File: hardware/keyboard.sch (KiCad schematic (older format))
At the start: 21 parts, among them J1 USB_OTG, J2 CONN_02X09, U1 ATMEGA32U4-AU, Y1 16MHz

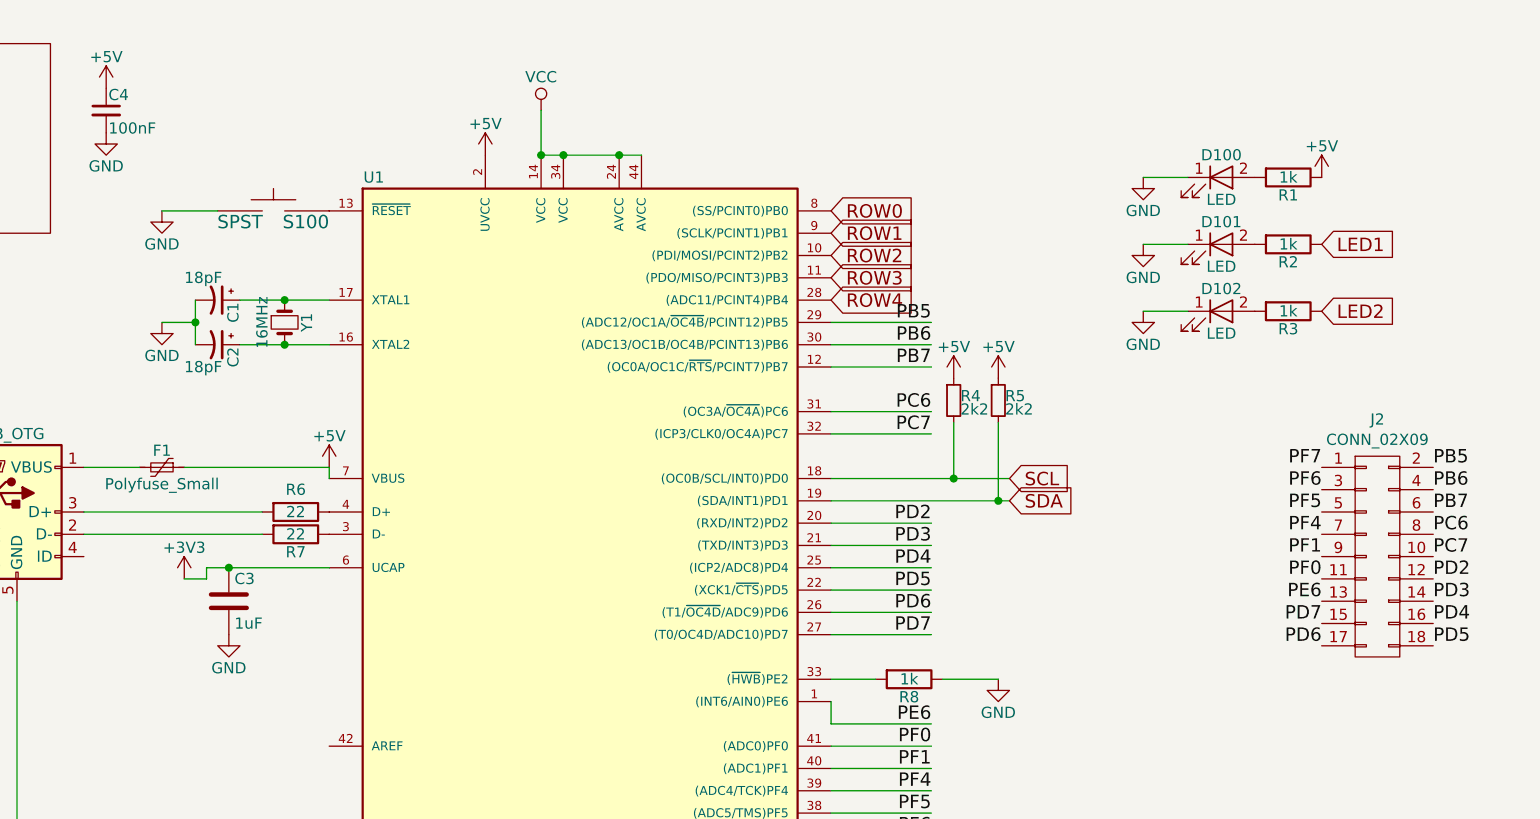
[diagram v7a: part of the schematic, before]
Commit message: Start to lay out components
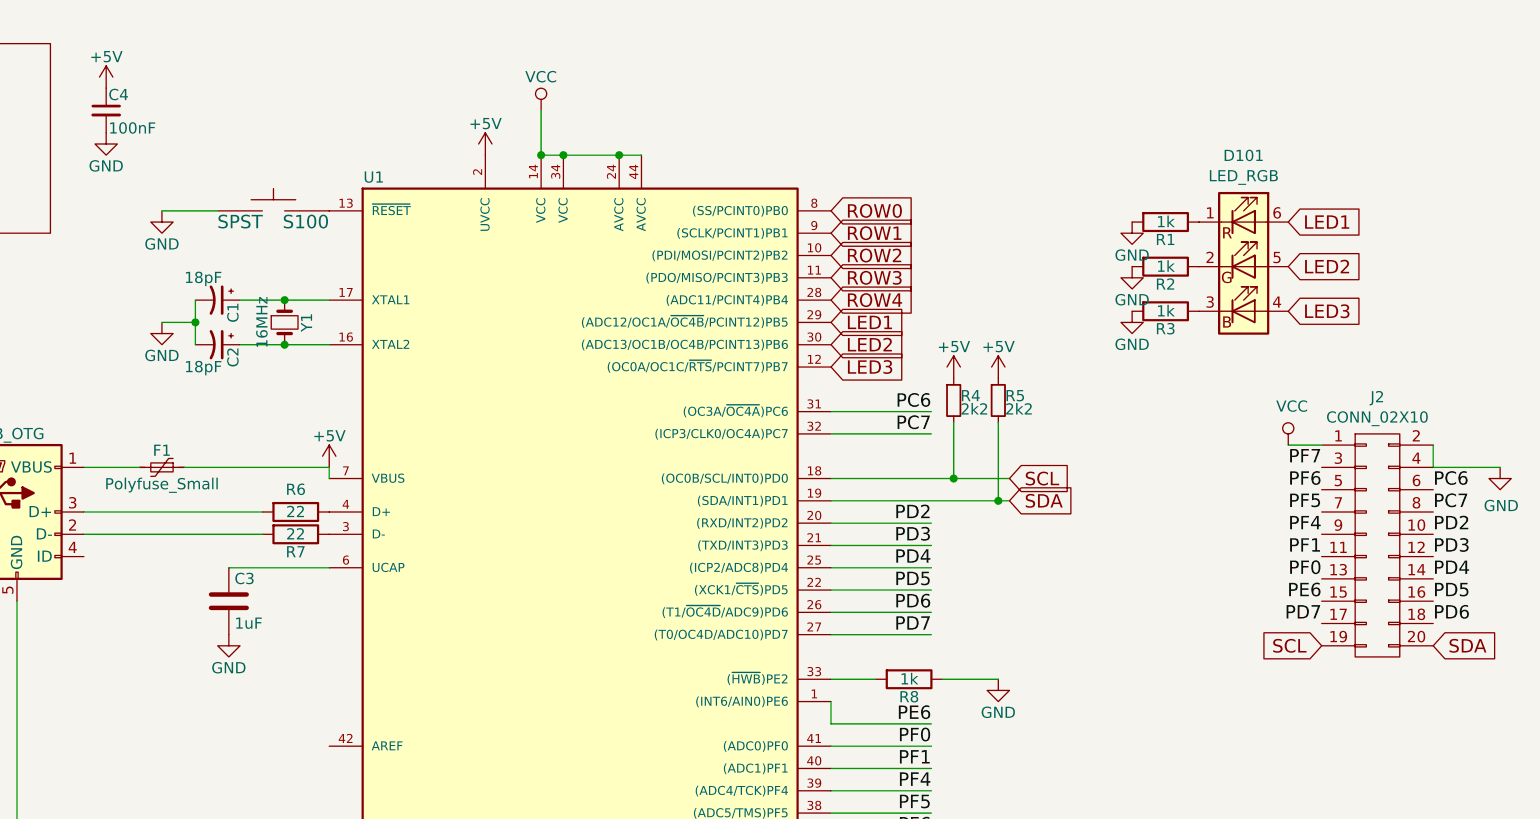
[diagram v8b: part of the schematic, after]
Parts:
- removed D100, D101, D102: LED, LEDs:LED_1206, symbol LED
- removed J2: CONN_02X09, keyboard-modules:pads, symbol CONN_02X09
- added D101: LED_RGB, LEDs:LED_RGB_5050-6, symbol LED_RGB
- added J2: CONN_02X10, keyboard-modules:ExpansionPads, symbol CONN_02X10
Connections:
- net PB5 is gone; now on net LED1: U1.29 ((ADC12/OC1A/~OC4B~/PCINT12)PB5)
- net PB6 is gone; now on net LED2: U1.30 ((ADC13/OC1B/OC4B/PCINT13)PB6)
- net +5V: no longer R1.1
- net GND: now also R1.2, R2.2, R3.2, J2.2 (P2), J2.4 (P4)
- net LED1: now also D101.6 (RA); no longer R2.1
- net LED2: now also D101.5 (GA); no longer R3.1
- net PC6: now also J2.6 (P6)
- net PC7: now also J2.8 (P8)
- net PD2: now also J2.10 (P10)
- net PD3: now also J2.12 (P12)
- net PD4: now also J2.14 (P14)
- net PD5: now also J2.16 (P16)
- net PD6: now also J2.18 (P18)
- net PD7: now also J2.17 (P17)
- net PE6: now also J2.15 (P15)
- net PF0: now also J2.13 (P13)
- net PF1: now also J2.11 (P11)
- net PF4: now also J2.9 (P9)
- net PF5: now also J2.7 (P7)
- net PF6: now also J2.5 (P5)
- net PF7: now also J2.3 (P3)
- net SCL: now also J2.19 (P19)
- net SDA: now also J2.20 (P20)
- net VCC: now also J2.1 (P1)
- net +3V3: no longer names the net of C3.1, U1.6 (UCAP)
- net PB7 renamed LED3
- net LED3: now also D101.4 (BA)
- new net: D101.1 (RK), R1.1
- new net: D101.2 (GK), R2.1
- new net: D101.3 (BK), R3.1
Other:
- moved on the sheet: R1, R2, R3
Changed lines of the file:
@@
 LIBS:valves
 LIBS:keyboard-cache
-EELAYER 25 0
+EELAYER 26 0
 EELAYER END
 $Descr A4 11693 8268
@@
 $EndComp
 $Comp
-L +3V3 #PWR04
-U 1 1 58EC69E9
-P 2150 3000
-F 0 "#PWR04" H 2150 2850 50  0001 C CNN
-F 1 "+3V3" H 2150 3140 50  0000 C CNN
-F 2 "" H 2150 3000 50  0001 C CNN
-F 3 "" H 2150 3000 50  0001 C CNN
-	1    2150 3000
-	1    0    0    -1
-$EndComp
-$Comp
-L LED D100
-U 1 1 58EC6D5A
-P 6800 1200
-F 0 "D100" H 6800 1300 50  0000 C CNN
-F 1 "LED" H 6800 1100 50  0000 C CNN
-F 2 "LEDs:LED_1206" H 6800 1200 50  0001 C CNN
-F 3 "" H 6800 1200 50  0001 C CNN
-	1    6800 1200
-	1    0    0    -1
-$EndComp
-$Comp
-L GND #PWR05
+L GND #PWR04
 U 1 1 58EC7101
-P 6450 1200
-F 0 "#PWR05" H 6450 950 50  0001 C CNN
-F 1 "GND" H 6450 1050 50  0000 C CNN
-F 2 "" H 6450 1200 50  0001 C CNN
-F 3 "" H 6450 1200 50  0001 C CNN
-	1    6450 1200
-	1    0    0    -1
-$EndComp
-$Comp
-L +5V #PWR06
-U 1 1 58EC7227
-P 7250 1200
-F 0 "#PWR06" H 7250 1050 50  0001 C CNN
-F 1 "+5V" H 7250 1340 50  0000 C CNN
-F 2 "" H 7250 1200 50  0001 C CNN
-F 3 "" H 7250 1200 50  0001 C CNN
-	1    7250 1200
+P 6400 1400
+F 0 "#PWR04" H 6400 1150 50  0001 C CNN
+F 1 "GND" H 6400 1250 50  0000 C CNN
+F 2 "" H 6400 1400 50  0001 C CNN
+F 3 "" H 6400 1400 50  0001 C CNN
+	1    6400 1400
 	1    0    0    -1
 $EndComp
@@
 L R R1
 U 1 1 58EC77A9
-P 7100 1200
-F 0 "R1" V 7180 1200 50  0000 C CNN
-F 1 "1k" V 7100 1200 50  0000 C CNN
-F 2 "Resistors_SMD:R_1206_HandSoldering" V 7030 1200 50  0001 C CNN
-F 3 "" H 7100 1200 50  0001 C CNN
-	1    7100 1200
+P 6550 1400
+F 0 "R1" V 6630 1400 50  0000 C CNN
+F 1 "1k" V 6550 1400 50  0000 C CNN
+F 2 "Resistors_SMD:R_1206_HandSoldering" V 6480 1400 50  0001 C CNN
+F 3 "" H 6550 1400 50  0001 C CNN
+	1    6550 1400
 	0    1    1    0
 $EndComp
@@
 $EndComp
 $Comp
-L GND #PWR07
+L GND #PWR05
 U 1 1 58EC962F
 P 2050 1850
-F 0 "#PWR07" H 2050 1600 50  0001 C CNN
+F 0 "#PWR05" H 2050 1600 50  0001 C CNN
 F 1 "GND" H 2050 1700 50  0000 C CNN
 F 2 "" H 2050 1850 50  0001 C CNN
@@
 $EndComp
 $Comp
-L +5V #PWR08
+L +5V #PWR06
 U 1 1 58ED0C76
 P 2800 2500
-F 0 "#PWR08" H 2800 2350 50  0001 C CNN
+F 0 "#PWR06" H 2800 2350 50  0001 C CNN
 F 1 "+5V" H 2800 2640 50  0000 C CNN
 F 2 "" H 2800 2500 50  0001 C CNN
@@
 $EndComp
 $Comp
-L +5V #PWR09
+L +5V #PWR07
 U 1 1 58ED0DA2
 P 3500 1100
-F 0 "#PWR09" H 3500 950 50  0001 C CNN
+F 0 "#PWR07" H 3500 950 50  0001 C CNN
 F 1 "+5V" H 3500 1240 50  0000 C CNN
 F 2 "" H 3500 1100 50  0001 C CNN
@@
 Connection ~ 3800 4500
 Wire Wire Line
-	2250 2950 2800 2950
-Wire Wire Line
-	2150 3000 2250 3000
-Wire Wire Line
-	2250 3000 2250 2950
-Connection ~ 2350 2950
-Wire Wire Line
-	6650 1200 6450 1200
+	2350 2950 2800 2950
 Wire Wire Line
 	2400 1750 2800 1750
@@
 Connection ~ 5800 2650
 $Comp
-L +5V #PWR010
+L +5V #PWR08
 U 1 1 594E98E9
 P 5600 2100
-F 0 "#PWR010" H 5600 1950 50  0001 C CNN
+F 0 "#PWR08" H 5600 1950 50  0001 C CNN
 F 1 "+5V" H 5600 2240 50  0000 C CNN
 F 2 "" H 5600 2100 50  0001 C CNN
@@
 $EndComp
 $Comp
-L +5V #PWR011
+L +5V #PWR09
 U 1 1 594E9917
 P 5800 2100
-F 0 "#PWR011" H 5800 1950 50  0001 C CNN
+F 0 "#PWR09" H 5800 1950 50  0001 C CNN
 F 1 "+5V" H 5800 2240 50  0000 C CNN
 F 2 "" H 5800 2100 50  0001 C CNN
@@
 $EndComp
 $Comp
-L LED D101
-U 1 1 594E9DFB
-P 6800 1500
-F 0 "D101" H 6800 1600 50  0000 C CNN
-F 1 "LED" H 6800 1400 50  0000 C CNN
-F 2 "LEDs:LED_1206" H 6800 1500 50  0001 C CNN
-F 3 "" H 6800 1500 50  0001 C CNN
-	1    6800 1500
-	1    0    0    -1
-$EndComp
-$Comp
-L GND #PWR012
+L GND #PWR010
 U 1 1 594E9E01
-P 6450 1500
-F 0 "#PWR012" H 6450 1250 50  0001 C CNN
-F 1 "GND" H 6450 1350 50  0000 C CNN
-F 2 "" H 6450 1500 50  0001 C CNN
-F 3 "" H 6450 1500 50  0001 C CNN
-	1    6450 1500
+P 6400 1600
+F 0 "#PWR010" H 6400 1350 50  0001 C CNN
+F 1 "GND" H 6400 1450 50  0000 C CNN
+F 2 "" H 6400 1600 50  0001 C CNN
+F 3 "" H 6400 1600 50  0001 C CNN
+	1    6400 1600
 	1    0    0    -1
 $EndComp
@@
 L R R2
 U 1 1 594E9E0D
-P 7100 1500
-F 0 "R2" V 7180 1500 50  0000 C CNN
-F 1 "1k" V 7100 1500 50  0000 C CNN
-F 2 "Resistors_SMD:R_1206_HandSoldering" V 7030 1500 50  0001 C CNN
-F 3 "" H 7100 1500 50  0001 C CNN
-	1    7100 1500
-	0    1    1    0
-$EndComp
-Wire Wire Line
-	6650 1500 6450 1500
-$Comp
-L LED D102
-U 1 1 594E9E7C
-P 6800 1800
-F 0 "D102" H 6800 1900 50  0000 C CNN
-F 1 "LED" H 6800 1700 50  0000 C CNN
-F 2 "LEDs:LED_1206" H 6800 1800 50  0001 C CNN
-F 3 "" H 6800 1800 50  0001 C CNN
-	1    6800 1800
-	1    0    0    -1
-$EndComp
-$Comp
-L GND #PWR013
+P 6550 1600
+F 0 "R2" V 6630 1600 50  0000 C CNN
+F 1 "1k" V 6550 1600 50  0000 C CNN
+F 2 "Resistors_SMD:R_1206_HandSoldering" V 6480 1600 50  0001 C CNN
+F 3 "" H 6550 1600 50  0001 C CNN
+	1    6550 1600
+	0    1    1    0
+$EndComp
+$Comp
+L GND #PWR011
 U 1 1 594E9E82
-P 6450 1800
-F 0 "#PWR013" H 6450 1550 50  0001 C CNN
-F 1 "GND" H 6450 1650 50  0000 C CNN
-F 2 "" H 6450 1800 50  0001 C CNN
-F 3 "" H 6450 1800 50  0001 C CNN
-	1    6450 1800
+P 6400 1800
+F 0 "#PWR011" H 6400 1550 50  0001 C CNN
+F 1 "GND" H 6400 1650 50  0000 C CNN
+F 2 "" H 6400 1800 50  0001 C CNN
+F 3 "" H 6400 1800 50  0001 C CNN
+	1    6400 1800
 	1    0    0    -1
 $EndComp
@@
 L R R3
 U 1 1 594E9E8E
-P 7100 1800
-F 0 "R3" V 7180 1800 50  0000 C CNN
-F 1 "1k" V 7100 1800 50  0000 C CNN
-F 2 "Resistors_SMD:R_1206_HandSoldering" V 7030 1800 50  0001 C CNN
-F 3 "" H 7100 1800 50  0001 C CNN
-	1    7100 1800
-	0    1    1    0
-$EndComp
-Wire Wire Line
-	6650 1800 6450 1800
-Text GLabel 7250 1500 2    60   Input ~ 0
+P 6550 1800
+F 0 "R3" V 6630 1800 50  0000 C CNN
+F 1 "1k" V 6550 1800 50  0000 C CNN
+F 2 "Resistors_SMD:R_1206_HandSoldering" V 6480 1800 50  0001 C CNN
+F 3 "" H 6550 1800 50  0001 C CNN
+	1    6550 1800
+	0    1    1    0
+$EndComp
+Text GLabel 7100 1400 2    60   Input ~ 0
 LED1
-Text GLabel 7250 1800 2    60   Input ~ 0
+Text GLabel 7100 1600 2    60   Input ~ 0
 LED2
 $Comp
@@
 	5050 3450 5250 3450
 $Comp
-L GND #PWR014
+L GND #PWR012
 U 1 1 594EA1C7
 P 5800 3450
-F 0 "#PWR014" H 5800 3200 50  0001 C CNN
+F 0 "#PWR012" H 5800 3200 50  0001 C CNN
 F 1 "GND" H 5800 3300 50  0000 C CNN
 F 2 "" H 5800 3450 50  0001 C CNN
@@
 	5550 3450 5800 3450
 $Comp
-L GND #PWR015
+L GND #PWR013
 U 1 1 594EA3EB
 P 2050 1350
-F 0 "#PWR015" H 2050 1100 50  0001 C CNN
+F 0 "#PWR013" H 2050 1100 50  0001 C CNN
 F 1 "GND" H 2050 1200 50  0000 C CNN
 F 2 "" H 2050 1350 50  0001 C CNN
@@
 	2300 1350 2050 1350
 Wire Wire Line
-	5050 1850 5500 1850
-Wire Wire Line
-	5050 1950 5500 1950
-Wire Wire Line
-	5050 2050 5500 2050
-Wire Wire Line
 	5050 2250 5500 2250
 Wire Wire Line
@@
 Wire Wire Line
 	5050 4250 5500 4250
-Text Label 5500 1850 2    60   ~ 0
-PB5
-Text Label 5500 1950 2    60   ~ 0
-PB6
-Text Label 5500 2050 2    60   ~ 0
-PB7
 Text Label 5500 2250 2    60   ~ 0
 PC6
@@
 Text Label 5500 4250 2    60   ~ 0
 PF7
-Text Label 7750 2500 0    60   ~ 0
-PB5
 Text Label 7750 2600 0    60   ~ 0
-PB6
+PC6
 Text Label 7750 2700 0    60   ~ 0
-PB7
+PC7
 Text Label 7750 2800 0    60   ~ 0
-PC6
+PD2
 Text Label 7750 2900 0    60   ~ 0
-PC7
+PD3
 Text Label 7750 3000 0    60   ~ 0
-PD2
+PD4
 Text Label 7750 3100 0    60   ~ 0
-PD3
+PD5
 Text Label 7750 3200 0    60   ~ 0
-PD4
-Text Label 7750 3300 0    60   ~ 0
-PD5
-Text Label 7250 3300 2    60   ~ 0
 PD6
 Text Label 7250 3200 2    60   ~ 0
@@
 $EndComp
 $Comp
-L +5V #PWR016
+L +5V #PWR014
 U 1 1 5955BD4A
 P 1800 800
-F 0 "#PWR016" H 1800 650 50  0001 C CNN
+F 0 "#PWR014" H 1800 650 50  0001 C CNN
 F 1 "+5V" H 1800 940 50  0000 C CNN
 F 2 "" H 1800 800 50  0001 C CNN
@@
 $EndComp
 $Comp
-L GND #PWR017
+L GND #PWR015
 U 1 1 5955BE42
 P 1800 1000
-F 0 "#PWR017" H 1800 750 50  0001 C CNN
+F 0 "#PWR015" H 1800 750 50  0001 C CNN
 F 1 "GND" H 1800 850 50  0000 C CNN
 F 2 "" H 1800 1000 50  0001 C CNN
@@
 $EndComp
 $Comp
-L CONN_02X09 J2
-U 1 1 595846BC
-P 7500 2900
+L LED_RGB D101
+U 1 1 595A9E52
+P 6900 1600
+F 0 "D101" H 6900 2097 50  0000 C CNN
+F 1 "LED_RGB" H 6900 2006 50  0000 C CNN
+F 2 "LEDs:LED_RGB_5050-6" H 6900 1550 50  0001 C CNN
+F 3 "" H 6900 1550 50  0001 C CNN
+	1    6900 1600
+	1    0    0    -1
+$EndComp
+Text GLabel 7100 1800 2    60   Input ~ 0
+LED3
+Text GLabel 5050 1850 2    60   Input ~ 0
+LED1
+Text GLabel 5050 1950 2    60   Input ~ 0
+LED2
+Text GLabel 5050 2050 2    60   Input ~ 0
+LED3
+$Comp
+L CONN_02X10 J2
+U 1 1 595ABD0A
+P 7500 2850
 F 0 "J2" H 7500 3515 50  0000 C CNN
-F 1 "CONN_02X09" H 7500 3424 50  0000 C CNN
-F 2 "keyboard-modules:pads" H 7500 1700 50  0001 C CNN
-F 3 "" H 7500 1700 50  0001 C CNN
-	1    7500 2900
-	1    0    0    -1
-$EndComp
+F 1 "CONN_02X10" H 7500 3424 50  0000 C CNN
+F 2 "keyboard-modules:ExpansionPads" H 7500 1650 50  0001 C CNN
+F 3 "" H 7500 1650 50  0001 C CNN
+	1    7500 2850
+	1    0    0    -1
+$EndComp
+Text GLabel 7250 3300 0    60   Input ~ 0
+SCL
+Text GLabel 7750 3300 2    60   Input ~ 0
+SDA
+$Comp
+L VCC #PWR016
+U 1 1 595ABF78
+P 7100 2400
+F 0 "#PWR016" H 7100 2250 50  0001 C CNN
+F 1 "VCC" H 7117 2573 50  0000 C CNN
+F 2 "" H 7100 2400 50  0001 C CNN
+F 3 "" H 7100 2400 50  0001 C CNN
+	1    7100 2400
+	1    0    0    -1
+$EndComp
+Wire Wire Line
+	7100 2400 7250 2400
+$Comp
+L GND #PWR017
+U 1 1 595AC06C
+P 8050 2500
+F 0 "#PWR017" H 8050 2250 50  0001 C CNN
+F 1 "GND" H 8055 2327 50  0000 C CNN
+F 2 "" H 8050 2500 50  0001 C CNN
+F 3 "" H 8050 2500 50  0001 C CNN
+	1    8050 2500
+	1    0    0    -1
+$EndComp
+Wire Wire Line
+	8050 2500 7750 2500
+Wire Wire Line
+	7750 2500 7750 2400
 $EndSCHEMATC
